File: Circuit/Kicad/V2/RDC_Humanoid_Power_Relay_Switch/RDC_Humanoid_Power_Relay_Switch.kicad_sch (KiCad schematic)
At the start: 16 parts, among them J1 XT60, J2 XT30, J3 Conn_01x02, Q1 PMOS, Q2 PMOS

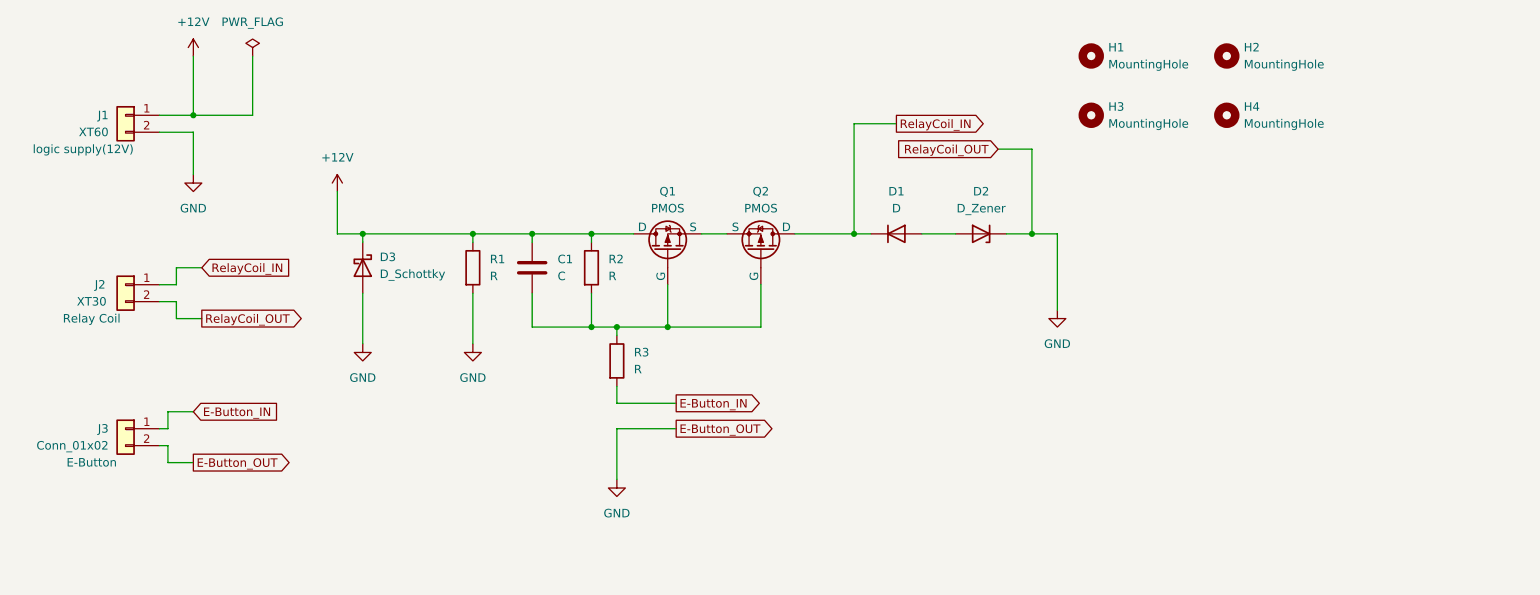
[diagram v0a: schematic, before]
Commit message: リレーコイルのスイッチ基板の回路図を起こした
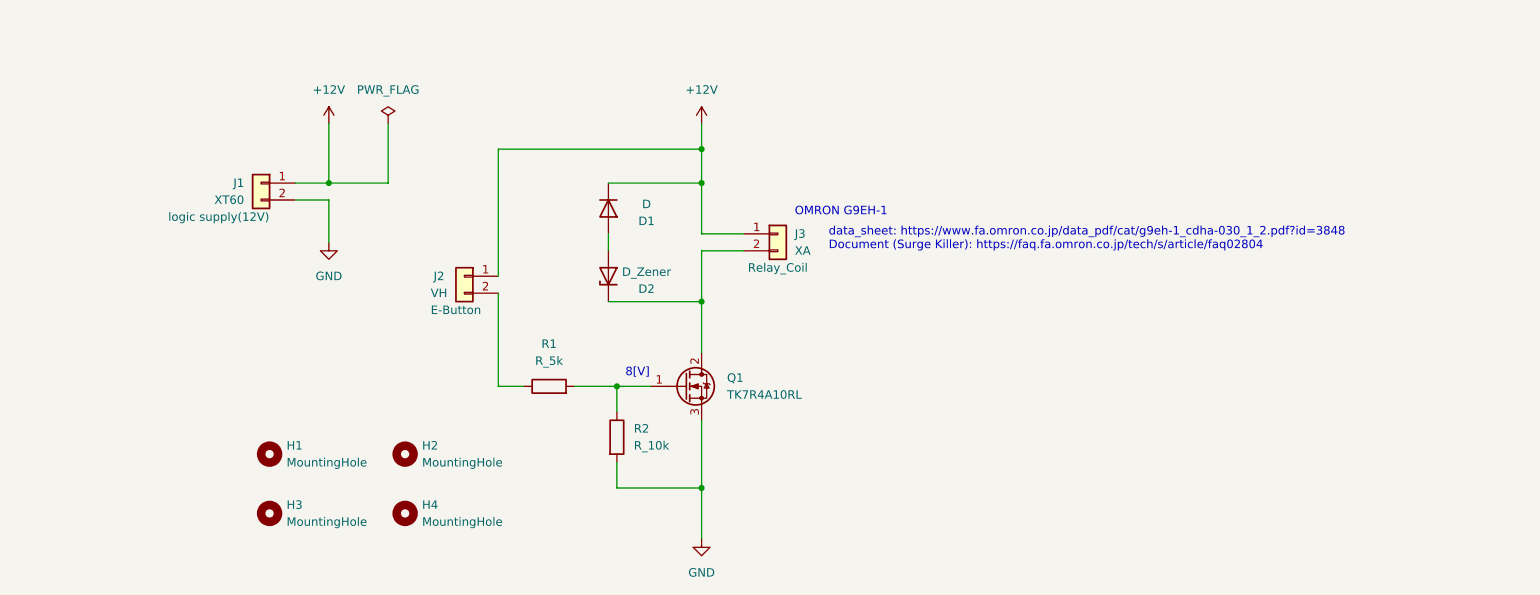
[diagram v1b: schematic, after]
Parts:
- removed C1: C, symbol Device:C
- removed D3: D_Schottky, symbol Device:D_Schottky
- removed Q1, Q2: PMOS, symbol Simulation_SPICE:PMOS
- removed R3: R, symbol Device:R
- added Q1: TK7R4A10RL, Package_TO_SOT_THT:TO-220-3_Vertical, symbol Device:Q_NMOS_GDS
- D1, D2: footprint (none) -> Diode_SMD:D_0603_1608Metric
- J2: value XT30 -> VH; footprint Connector_AMASS:AMASS_XT30U-M_1x02_P5.0mm_Vertical -> Connector_JST:JST_VH_B2P-VH_1x02_P3.96mm_Vertical; description Relay Coil -> E-Button
- J3: value Conn_01x02 -> XA; footprint Connector_AMASS:AMASS_XT30PW-M_1x02_P2.50mm_Horizontal -> Connector_JST:JST_XA_B02B-XASK-1_1x02_P2.50mm_Vertical; description E-Button -> Relay_Coil
- R1: value R -> R_5k; footprint (none) -> Resistor_SMD:R_0603_1608Metric
- R2: value R -> R_10k; footprint (none) -> Resistor_SMD:R_0603_1608Metric
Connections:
- net E-Button_IN is gone; now on net +12V: J3.1 (Pin_1)
- net RelayCoil_IN is gone; now on net +12V: D1.1 (K), J2.1 (Pin_1)
- net +12V: no longer R1.1, R2.1
- net GND: now also R2.2, Q1.3 (S); no longer D2.1 (K), J2.2 (Pin_2), J3.2 (Pin_2), R1.2
- new net: Q1.1 (G), R1.2, R2.1
- new net: D2.1 (K), J3.2 (Pin_2), Q1.2 (D)
- new net: J2.2 (Pin_2), R1.1
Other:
- note added: "8[V]"
- note added: "OMRON G9EH-1"
- note added: "data_sheet: https://www.fa.omron.co.jp/data_pdf/cat/g9eh-1_cdha-030_1_2.pdf?id=3848 Document (Surge Killer): https://faq.fa.omron.co.jp/tech/s/article/faq02804"
- moved on the sheet: H1, H2, H3, H4, J1, J3

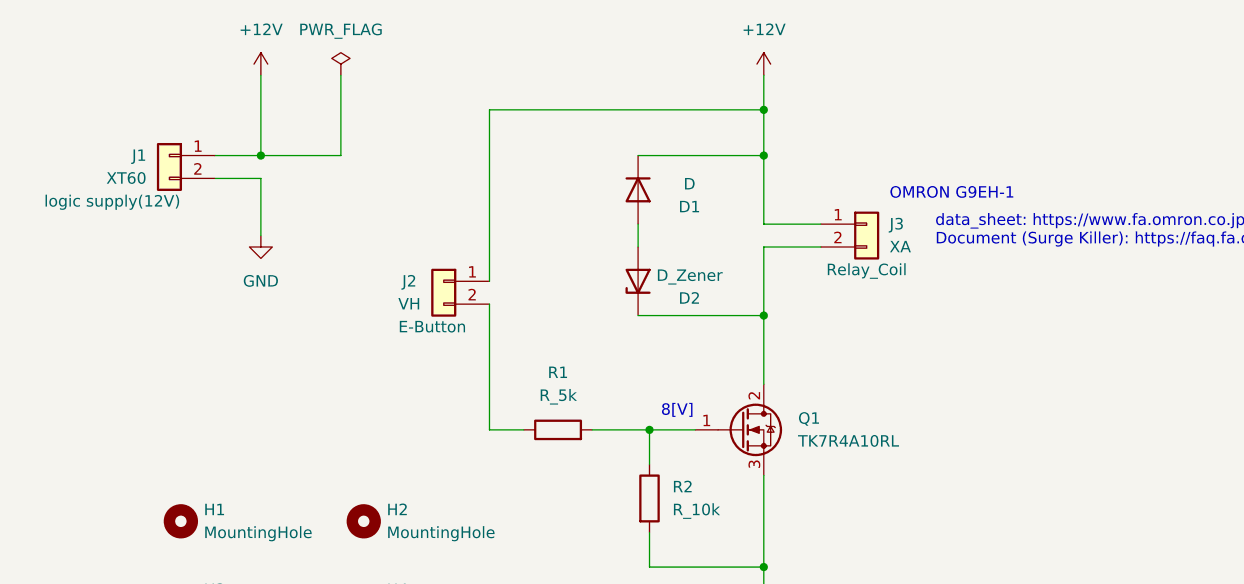
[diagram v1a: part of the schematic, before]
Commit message: Relay_Switchの回路図とPCBを組んでみた。
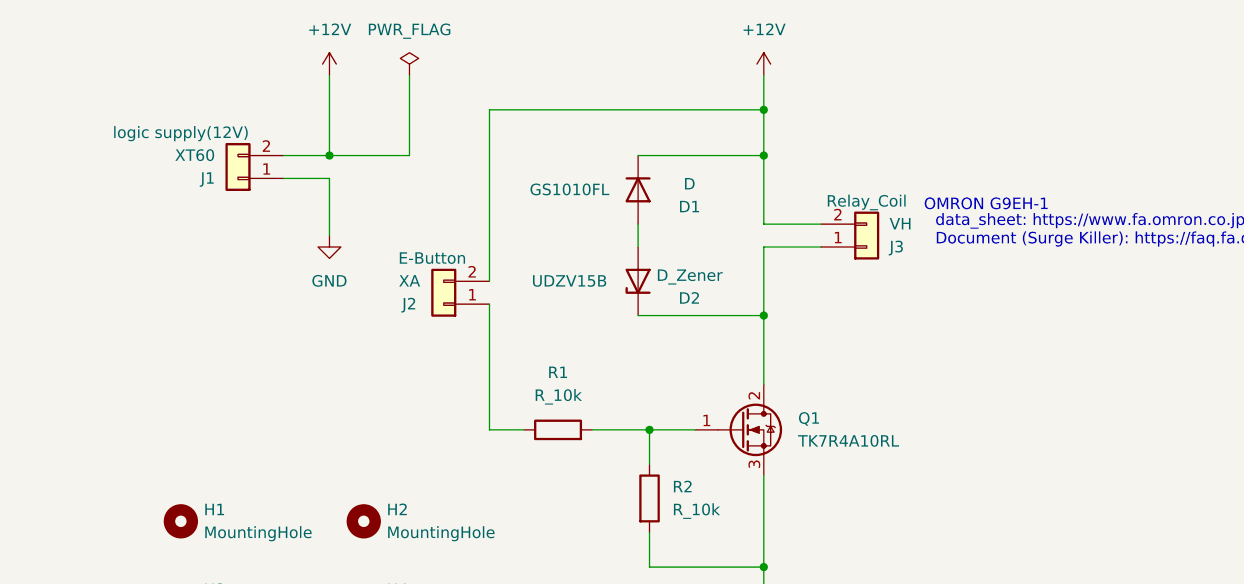
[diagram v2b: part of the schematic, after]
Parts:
- D1: footprint Diode_SMD:D_0603_1608Metric -> Diode_SMD:D_SOD-123; name (none) -> GS1010FL
- D2: footprint Diode_SMD:D_0603_1608Metric -> Diode_SMD:D_SOD-323; name (none) -> UDZV15B
- J2: value VH -> XA; footprint Connector_JST:JST_VH_B2P-VH_1x02_P3.96mm_Vertical -> Connector_JST:JST_XA_S02B-XASK-1_1x02_P2.50mm_Horizontal
- J3: value XA -> VH; footprint Connector_JST:JST_XA_B02B-XASK-1_1x02_P2.50mm_Vertical -> Connector_JST:JST_VH_B2P-VH_1x02_P3.96mm_Vertical
- R1: value R_5k -> R_10k
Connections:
- net +12V: now also J1.2 (Pin_2), J2.2 (Pin_2), J3.2 (Pin_2); no longer J1.1 (Pin_1), J2.1 (Pin_1), J3.1 (Pin_1)
- net GND: now also J1.1 (Pin_1); no longer J1.2 (Pin_2)
- net at D2.1 (K), Q1.2 (D): now also J3.1 (Pin_1); no longer J3.2 (Pin_2)
- net at R1.1: now also J2.1 (Pin_1); no longer J2.2 (Pin_2)
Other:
- note removed: "8[V]"
- moved on the sheet: J1, J2

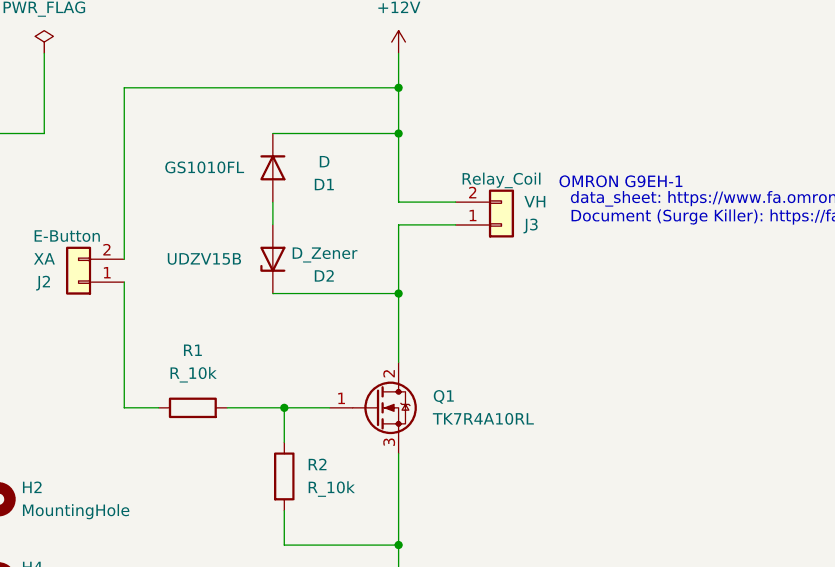
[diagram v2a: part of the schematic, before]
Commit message: アドバイスを元に修正。Relay Switch用の基板ができた。
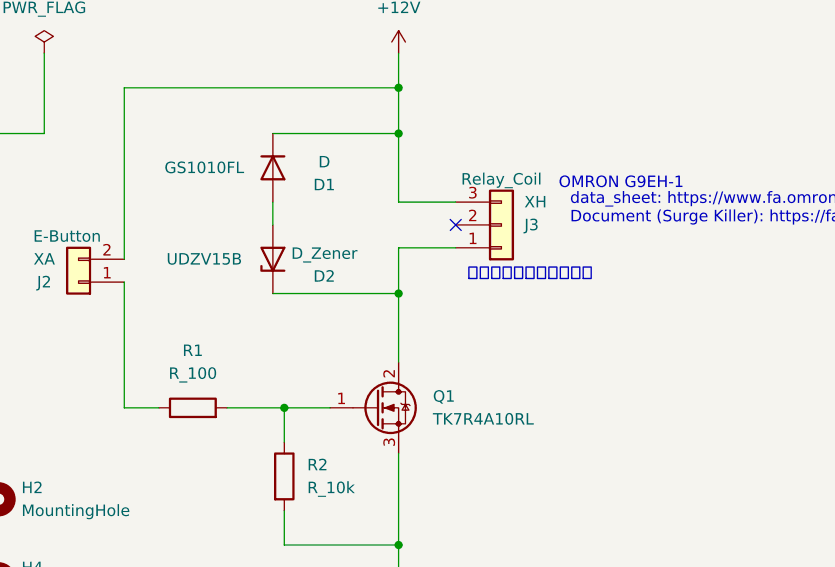
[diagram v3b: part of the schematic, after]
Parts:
- J3: value VH -> XH; footprint Connector_JST:JST_VH_B2P-VH_1x02_P3.96mm_Vertical -> Connector_JST:JST_XH_B3B-XH-A_1x03_P2.50mm_Vertical; symbol Connector_Generic:Conn_01x02 -> Connector_Generic:Conn_01x03
- R1: value R_10k -> R_100
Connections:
- net +12V: now also J3.3 (Pin_3); no longer J3.2 (Pin_2)
- no-connect marks 0 -> 1
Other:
- note added: "抜けにくさ、誤接続防止"
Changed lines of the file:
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@@
   (junction (at 85.09 46.99) (diameter 0) (color 0 0 0 0)
   )
-  (wire (pts (xy 133.35 57.15) (xy 133.35 64.77))
+  (no_connect (at 139.7 57.15))
+  (wire (pts (xy 139.7 59.69) (xy 133.35 59.69))
+    (stroke (width 0) (type default))
+  )
+  (wire (pts (xy 133.35 59.69) (xy 133.35 64.77))
     (stroke (width 0) (type default))
   )
@@
     (stroke (width 0) (type default))
   )
-  (wire (pts (xy 139.7 57.15) (xy 133.35 57.15))
-    (stroke (width 0) (type default))
-  )
   (wire (pts (xy 102.87 77.47) (xy 106.68 77.47))
     (stroke (width 0) (type default))
@@
   (wire (pts (xy 119.38 54.61) (xy 119.38 57.15))
     (stroke (width 0) (type default))
+  )
+  (text "抜けにくさ、誤接続防止" (at 140.97 63.5 0)
+    (effects (font (size 1.27 1.27)) (justify left bottom))
   )
   (text "data_sheet: https://www.fa.omron.co.jp/data_pdf/cat/g9eh-1_cdha-030_1_2.pdf?id=3848\nDocument (Surge Killer): https://faq.fa.omron.co.jp/tech/s/article/faq02804"
@@
     )
   )
-  (symbol (lib_id "Connector_Generic:Conn_01x02") (at 144.78 57.15 0) (mirror x) (unit 1)
+  (symbol (lib_id "Connector_Generic:Conn_01x03") (at 144.78 57.15 0) (mirror x) (unit 1)
     (in_bom yes) (on_board yes) (dnp no)
     (property "Reference" "J3" (at 147.32 57.15 0)
       (effects (font (size 1.27 1.27)) (justify left))
     )
-    (property "Value" "VH" (at 147.32 54.61 0)
-      (effects (font (size 1.27 1.27)) (justify left))
-    )
-    (property "Footprint" "Connector_JST:JST_VH_B2P-VH_1x02_P3.96mm_Vertical" (at 144.78 57.15 0)
+    (property "Value" "XH" (at 147.32 54.61 0)
+      (effects (font (size 1.27 1.27)) (justify left))
+    )
+    (property "Footprint" "Connector_JST:JST_XH_B3B-XH-A_1x03_P2.50mm_Vertical" (at 144.78 57.15 0)
       (effects (font (size 1.27 1.27)) hide)
     )
@@
     (pin "1")
     (pin "2")
+    (pin "3")
     (instances
       (project "RDC_Humanoid_Power_Relay_Switch"
@@
       (effects (font (size 1.27 1.27)))
     )
-    (property "Value" "R_10k" (at 110.49 73.66 90)
-      (effects (font (size 1.27 1.27)))
-    )
+    (property "Value" "R_100" (at 110.49 73.66 90)
+      (effects (font (size 1.27 1.27)))
+    )

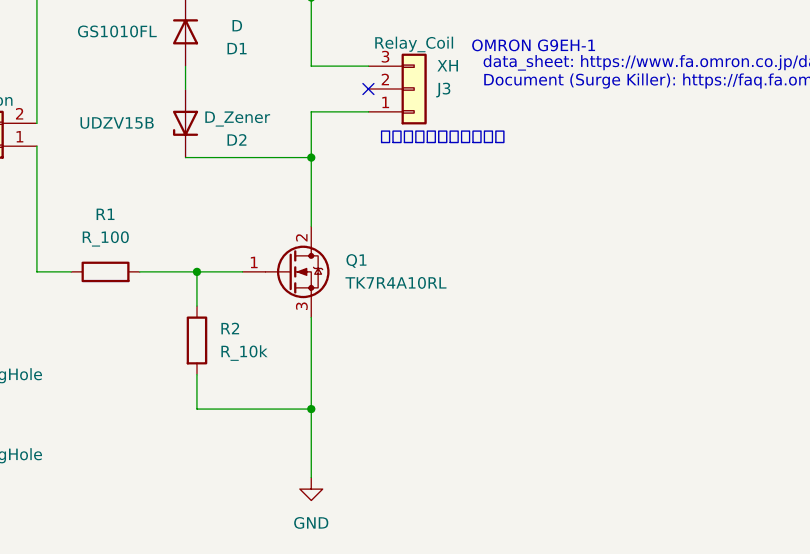
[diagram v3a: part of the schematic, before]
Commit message: 回路図のコメントの修正
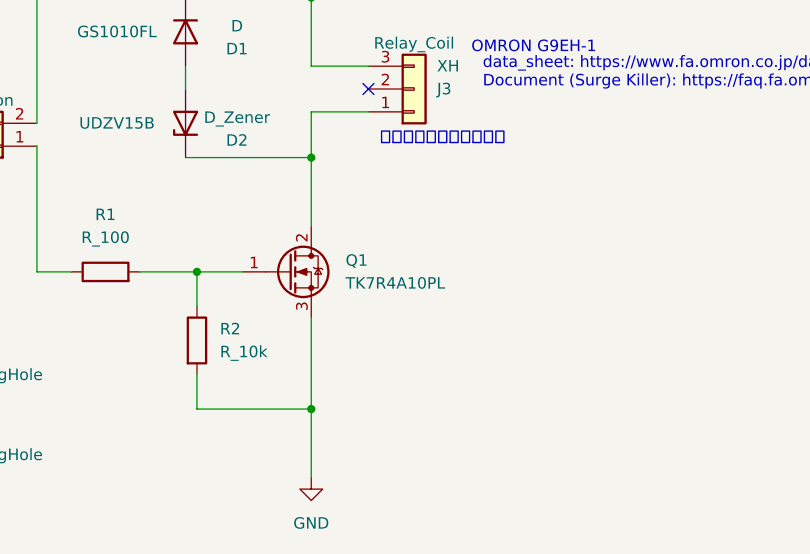
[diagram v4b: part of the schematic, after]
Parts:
- Q1: value TK7R4A10RL -> TK7R4A10PL
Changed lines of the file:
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@@
       (effects (font (size 1.27 1.27)) (justify left))
     )
-    (property "Value" "TK7R4A10RL" (at 137.16 78.74 0)
+    (property "Value" "TK7R4A10PL" (at 137.16 78.74 0)
       (effects (font (size 1.27 1.27)) (justify left))
     )
